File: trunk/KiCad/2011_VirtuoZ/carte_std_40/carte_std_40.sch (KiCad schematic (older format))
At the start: 4 parts, among them P1 ALIM, U1 7805

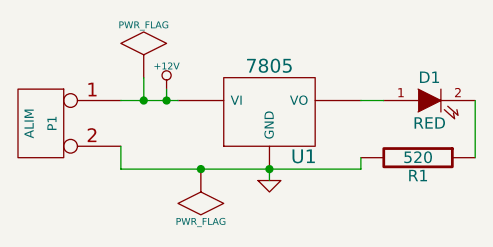
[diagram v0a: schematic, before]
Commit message: 
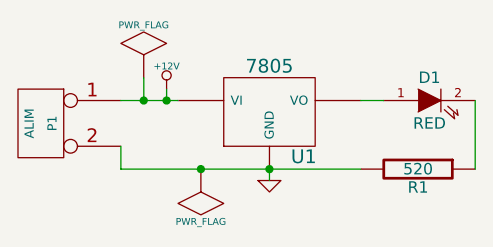
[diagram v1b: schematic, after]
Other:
- moved on the sheet: R1
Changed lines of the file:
@@
-EESchema Schematic File Version 2  date 04/12/2010 17:33:25
+EESchema Schematic File Version 2  date 04/12/2010 17:37:03
 LIBS:power
 LIBS:device
@@
 $EndDescr
 Wire Wire Line
-	2050 2450 3100 2450
-Connection ~ 2250 2150
+	3600 2450 3600 2150
+Connection ~ 2400 2450
 Wire Wire Line
-	2250 2150 2250 2100
-Connection ~ 2700 2450
+	2700 2450 2700 2500
 Wire Wire Line
-	3600 2150 3600 2400
-Connection ~ 2150 2150
+	3200 2150 3100 2150
 Wire Wire Line
-	2150 2050 2150 2150
+	2050 2350 2050 2450
 Wire Wire Line
 	2300 2150 2050 2150
 Wire Wire Line
-	2050 2450 2050 2350
+	2150 2050 2150 2150
+Connection ~ 2150 2150
+Connection ~ 2700 2450
 Wire Wire Line
-	3200 2150 3100 2150
+	2250 2150 2250 2100
+Connection ~ 2250 2150
 Wire Wire Line
-	2700 2450 2700 2500
-Wire Wire Line
-	3100 2450 3100 2400
-Connection ~ 2400 2450
+	2050 2450 3100 2450
 $Comp
 L R R1
 U 1 1 4CFA685A
-P 3350 2400
-F 0 "R1" V 3430 2400 50  0000 C CNN
-F 1 "520" V 3350 2400 50  0000 C CNN
-	1    3350 2400
+P 3350 2450
+F 0 "R1" V 3430 2450 50  0000 C CNN
+F 1 "520" V 3350 2450 50  0000 C CNN
+	1    3350 2450
 	0    1    1    0
 $EndComp
